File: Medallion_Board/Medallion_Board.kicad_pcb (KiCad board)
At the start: 4 copper layers, 70 x 115.3 mm, 80 parts, among them IC1 Wio-SX1262, J1 SWD HEADER, J2 EXPANSION, P1 JST_BTN_1, P2 JST_BTN_2, P3 JST_BTN_3, Q1 DMG3415U, U1 MDBT50Q-1MV2, U2 MAX17048G_T10, U3 LC86LICMD, U4 RT9080-33GJ5, U5 MCP73831T-2ACI_OT, U6 BNO085, X1 USB4085-GF-A, Y1 32.768KHZ

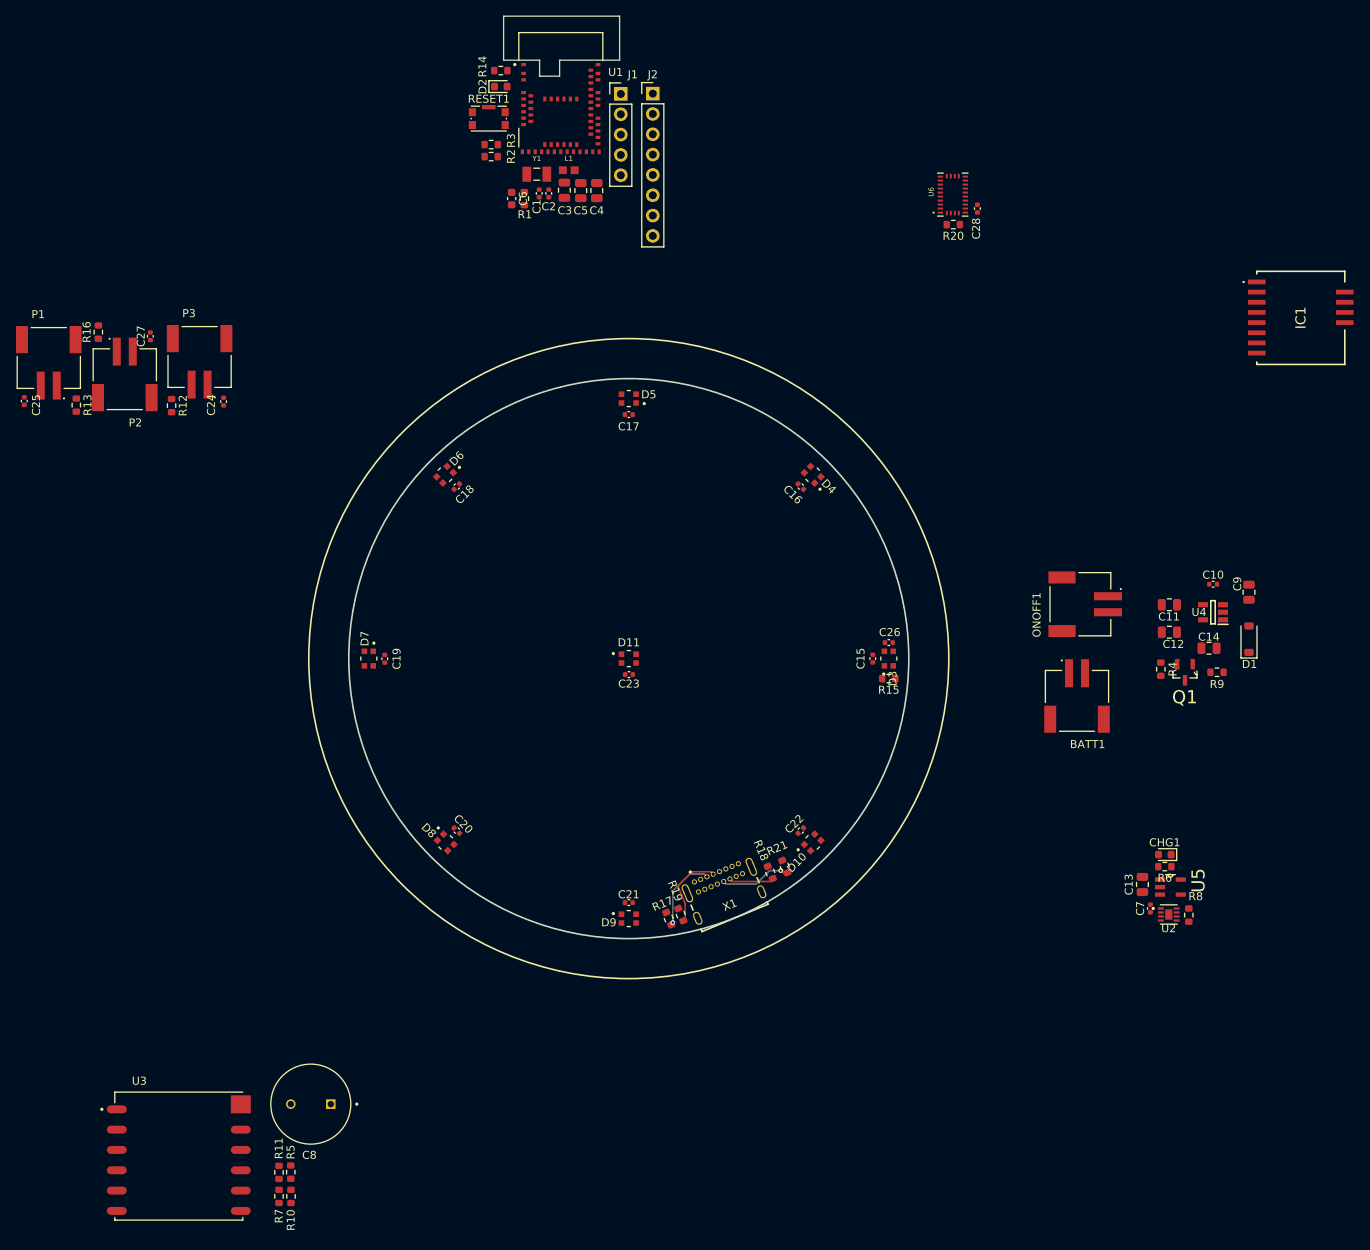
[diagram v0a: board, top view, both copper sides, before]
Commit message: Main board design is in place. Needs haptics and buzzer
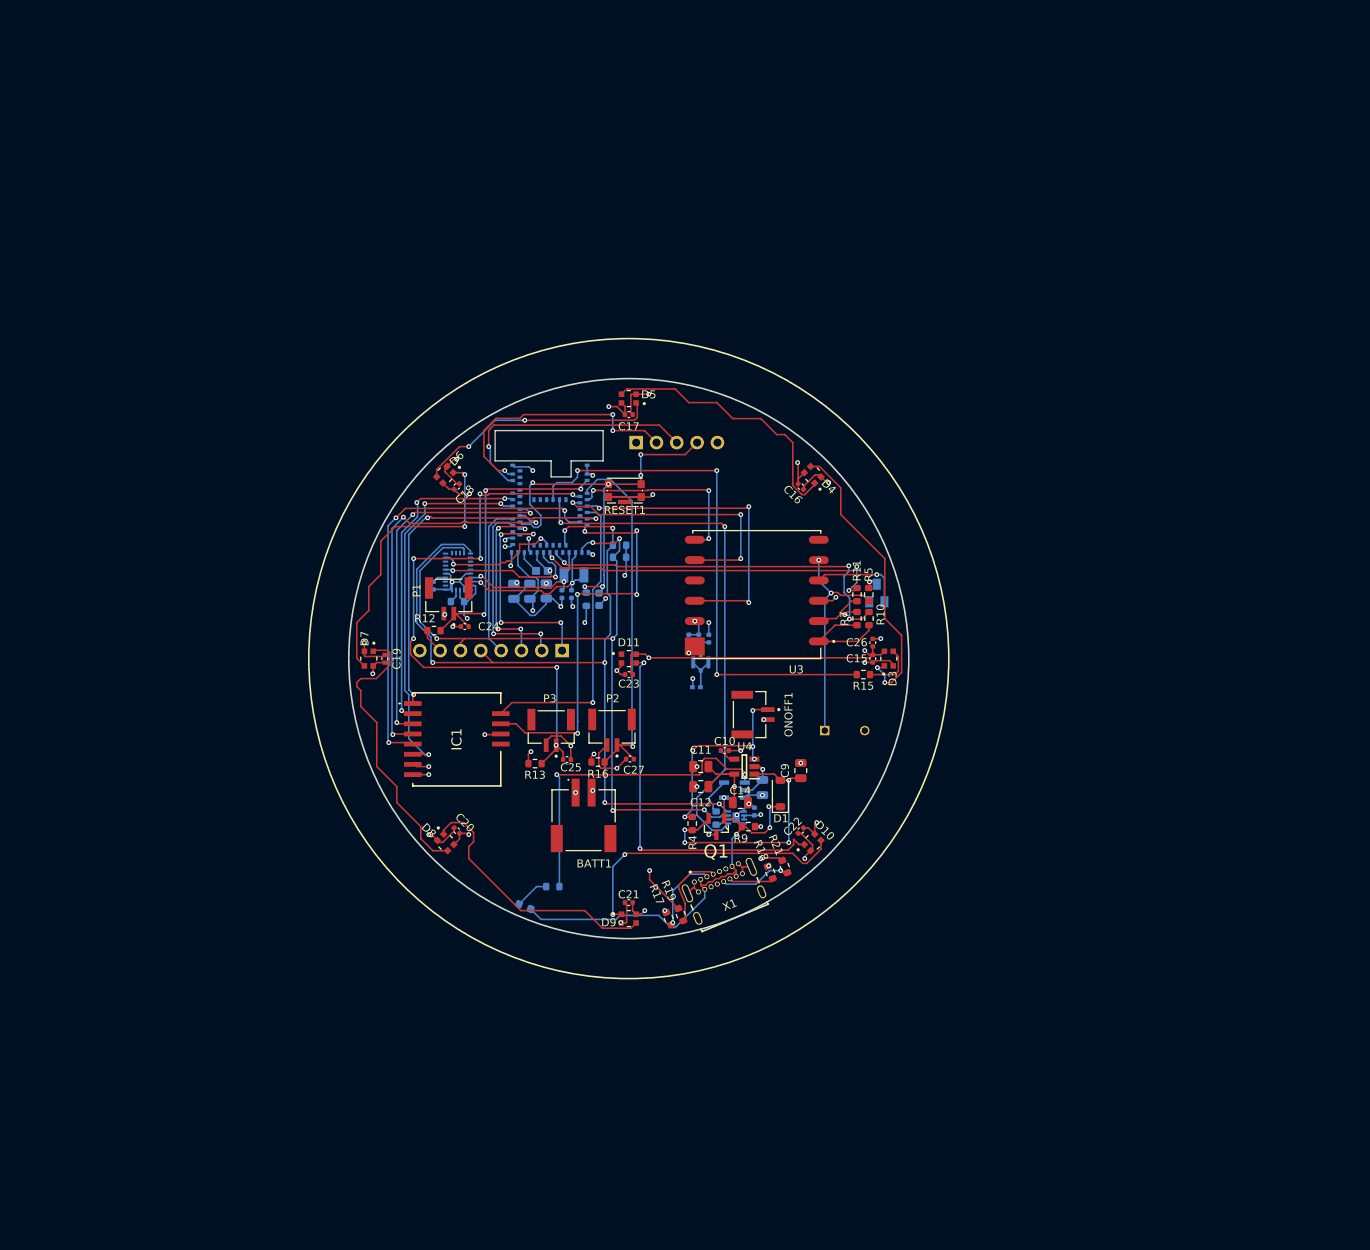
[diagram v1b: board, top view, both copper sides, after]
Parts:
- added C29: NM, Capacitor_SMD:C_0402_1005Metric, B.Cu at (110.0, 97.5)
- added C30: NM, Capacitor_SMD:C_0402_1005Metric, B.Cu at (107.5, 97.5)
- added D12: TPD1E05U06DPYR, TPD1E05U06DPYR:DIO_TPD1E05U06DPYR, B.Cu at (108.5, 103.6)
- added J3: IPEX, RECE.20369:RECE20369001E01, B.Cu at (109.0, 100.5)
- C1, C13, C2, C28, C3, C4, C5, C6, C7, C8, CHG1, J1, J2, L1, R1, R2, R20, R3, R6, R8, U1, U2, U5, U6, Y1: moved to B.Cu
- D2: value RED -> BAV199; footprint LED_SMD:LED_0603_1608Metric -> BAV199:SOT23; moved to B.Cu
- ONOFF1, P1, P2, P3: footprint S2B-PH-SM4-TB_LF__SN_:JST_S2B-PH-SM4-TB_LF__SN_ -> SM02B-GHS-TB:JST_SM02B-GHS-TB
- R14: value 5K -> 0R; footprint Resistor_SMD:R_0603_1608Metric -> Resistor_SMD:R_0402_1005Metric; moved to B.Cu
- moved IC1 117.9 mm to (78.5, 110.1)
- moved R10 102.2 mm to (130.0, 95.0)
- moved R11 102.2 mm to (128.5, 92.0)
- moved R7 102.2 mm to (128.5, 95.0)
- moved R5 102.1 mm to (130.0, 92.0)
- moved U3 100.7 mm to (116.0, 92.0), turned to 180 degrees
- moved C28 82.7 mm to (75.6, 90.9)
- moved R16 82.4 mm to (96.2, 112.9), turned to 180 degrees
- moved C8 81.5 mm to (127.0, 109.0), turned to 0 degrees
- moved C25 81.3 mm to (92.3, 112.6), turned to 180 degrees
- moved CHG1 80.3 mm to (87.0, 131.0), turned to -22.5 degrees
- moved C27 79.9 mm to (100.2, 112.6), turned to 0 degrees
- moved D2 78.8 mm to (131.0, 91.8), turned to 180 degrees
- moved R20 77.9 mm to (78.6, 92.9), turned to 0 degrees
- moved U6 77.8 mm to (78.7, 89.1)
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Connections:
- D2 pad 1: GND -> 3.3V
- D2 pad 2: Net-(D2-Pad2) -> unconnected-(D2-Pad2)
- R14 pad 1: /STATUS_LED -> Net-(J3-CENTRE)
- R14 pad 2: Net-(D2-Pad2) -> Net-(U3-EX_ANT)
- R5 pad 1: 3.3V -> Net-(D2-Pad3)
- U1 pad 59: /STATUS_LED -> unconnected-(U1-P1.05-Pad59)
- U3 pad 11: unconnected-(U3-EX_ANT-Pad11) -> Net-(U3-EX_ANT)
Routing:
- net VBAT: track 0.00 -> 313.1 mm, vias 0 -> 13
- net GND: track 0.00 -> 125.0 mm, vias 0 -> 42
- net /SDA: track 0.00 -> 103.7 mm, vias 0 -> 6
- net VBUS: track 0.00 -> 100.2 mm, vias 0 -> 5
- net /SCL: track 0.00 -> 95.9 mm, vias 0 -> 6
- net /USER_BTN_3: track 0.00 -> 74.9 mm, vias 0 -> 7
- net /NEOPIX: track 0.00 -> 66.4 mm, vias 0 -> 3
- net /LOW_BATT: track 0.00 -> 66.2 mm, vias 0 -> 2
- net /D+: track 0.00 -> 60.7 mm, vias 0 -> 2
- net /D-: track 0.00 -> 60.6 mm, vias 0 -> 2
- net /LORA_NRST: track 0.00 -> 56.1 mm, vias 0 -> 3
- net 3.3V: track 0.00 -> 52.0 mm, vias 0 -> 10
- net /uC_RESET: track 0.00 -> 51.1 mm, vias 0 -> 6
- net /LORA_BUSY: track 0.00 -> 50.6 mm, vias 0 -> 5
- net /SPI_SCK: track 0.00 -> 49.7 mm, vias 0 -> 3
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- added copper zone on In1.Cu, net 3.3V
- added copper zone on In2.Cu, net GND
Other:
- board size 70 x 115.3 mm -> 70 x 70 mm

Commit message: v1.0 pcb design
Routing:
- net /VHI: track 32.2 -> 34.7 mm
- net GND: track 125.0 -> 126.3 mm, vias 42 -> 41
- net VBUS: track 100.2 -> 100.6 mm, vias 5 -> 6
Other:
- outline, holes or cut-outs redrawn
- board text added: "3.3V"
- board text added: "GND"
- board text added: "IO14"
- board text added: "IO15"
- board text added: "IO16"
- board text added: "IO17"
- board text added: "Jim Wild 2026"
- board text added: "RST"
- board text added: "SCL"
- board text added: "SDA"
- board text added: "SWDCLK"
- board text added: "SWDIO"
- board text added: "v1.0"

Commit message: Some notes. Figuring out costs
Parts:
- C8: moved to F.Cu
- moved C8 44.6 mm to (84.5, 122.5), turned to -90 degrees
- moved C20 3.00 mm to (78.5, 124.5), turned to -135 degrees
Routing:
- net Net-(U3-V_BCKP): track 27.5 -> 80.1 mm, vias 2 -> 4
- net GND: track 126.3 -> 136.9 mm
